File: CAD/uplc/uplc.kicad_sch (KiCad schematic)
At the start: 32 parts, among them J1 Conn_01x06_Pin, J2 SM12B-GHS-TB(LF)(SN), K1 G6K-2F-Y, K2 G6K-2F-Y, U1 DS8242-33S5, U3 ESP32-C3-WROOM-02, U5 TBD62003AFWG, Y1 32.568khz

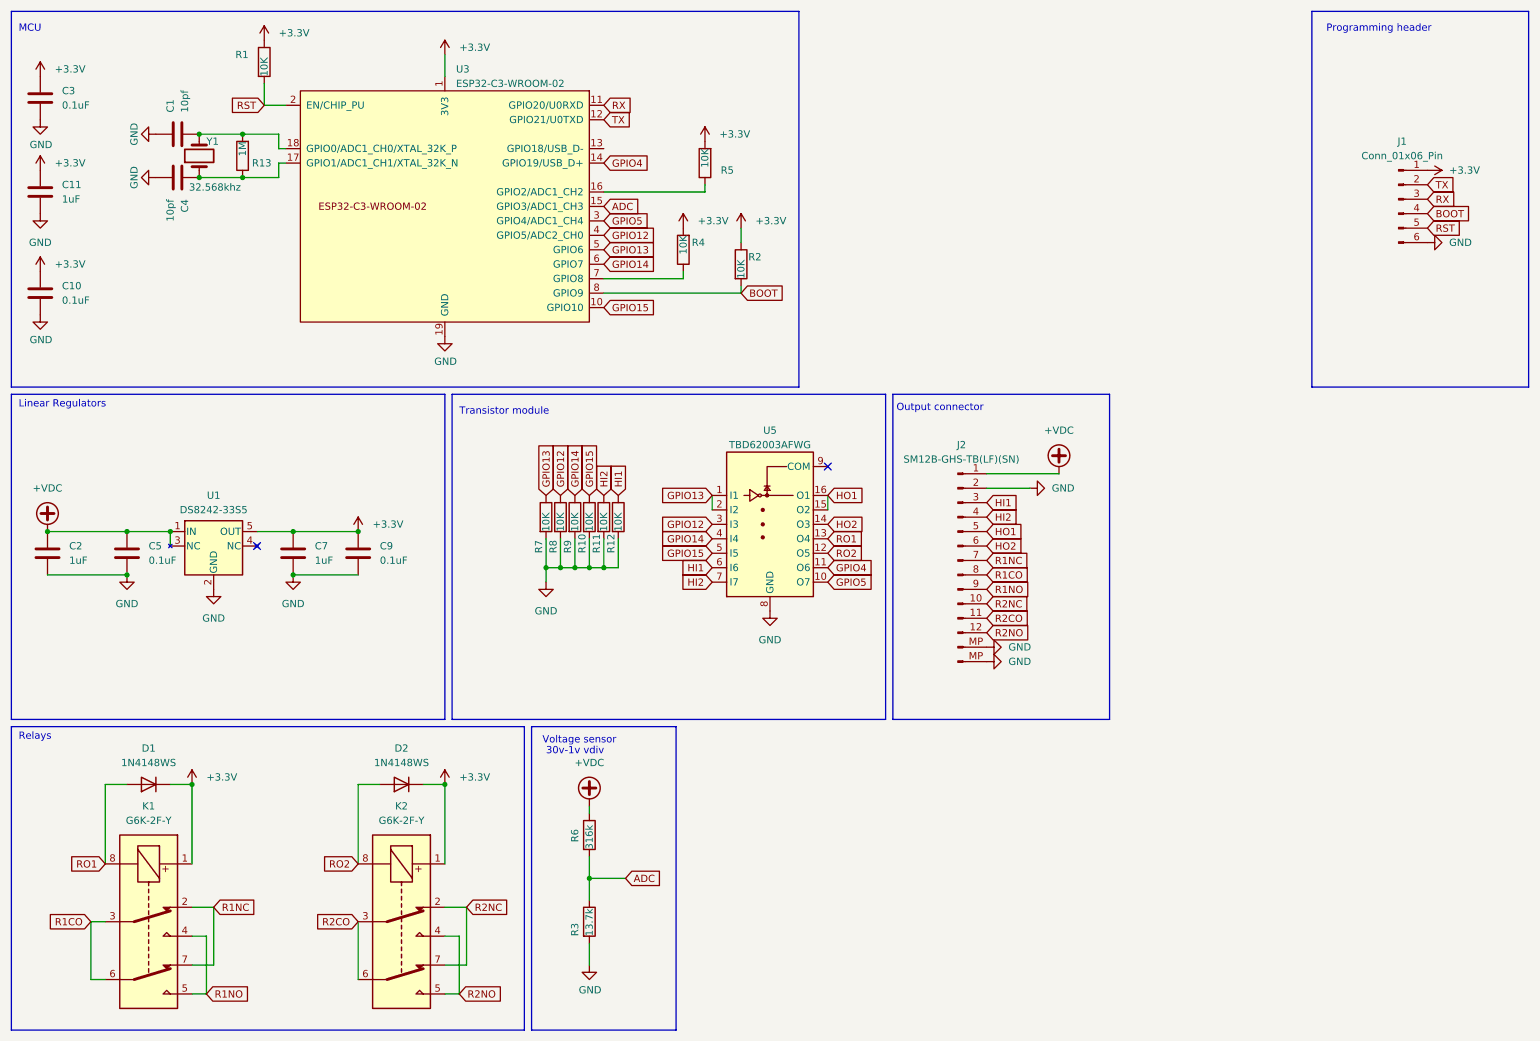
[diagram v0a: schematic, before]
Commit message: Pin Rearangement
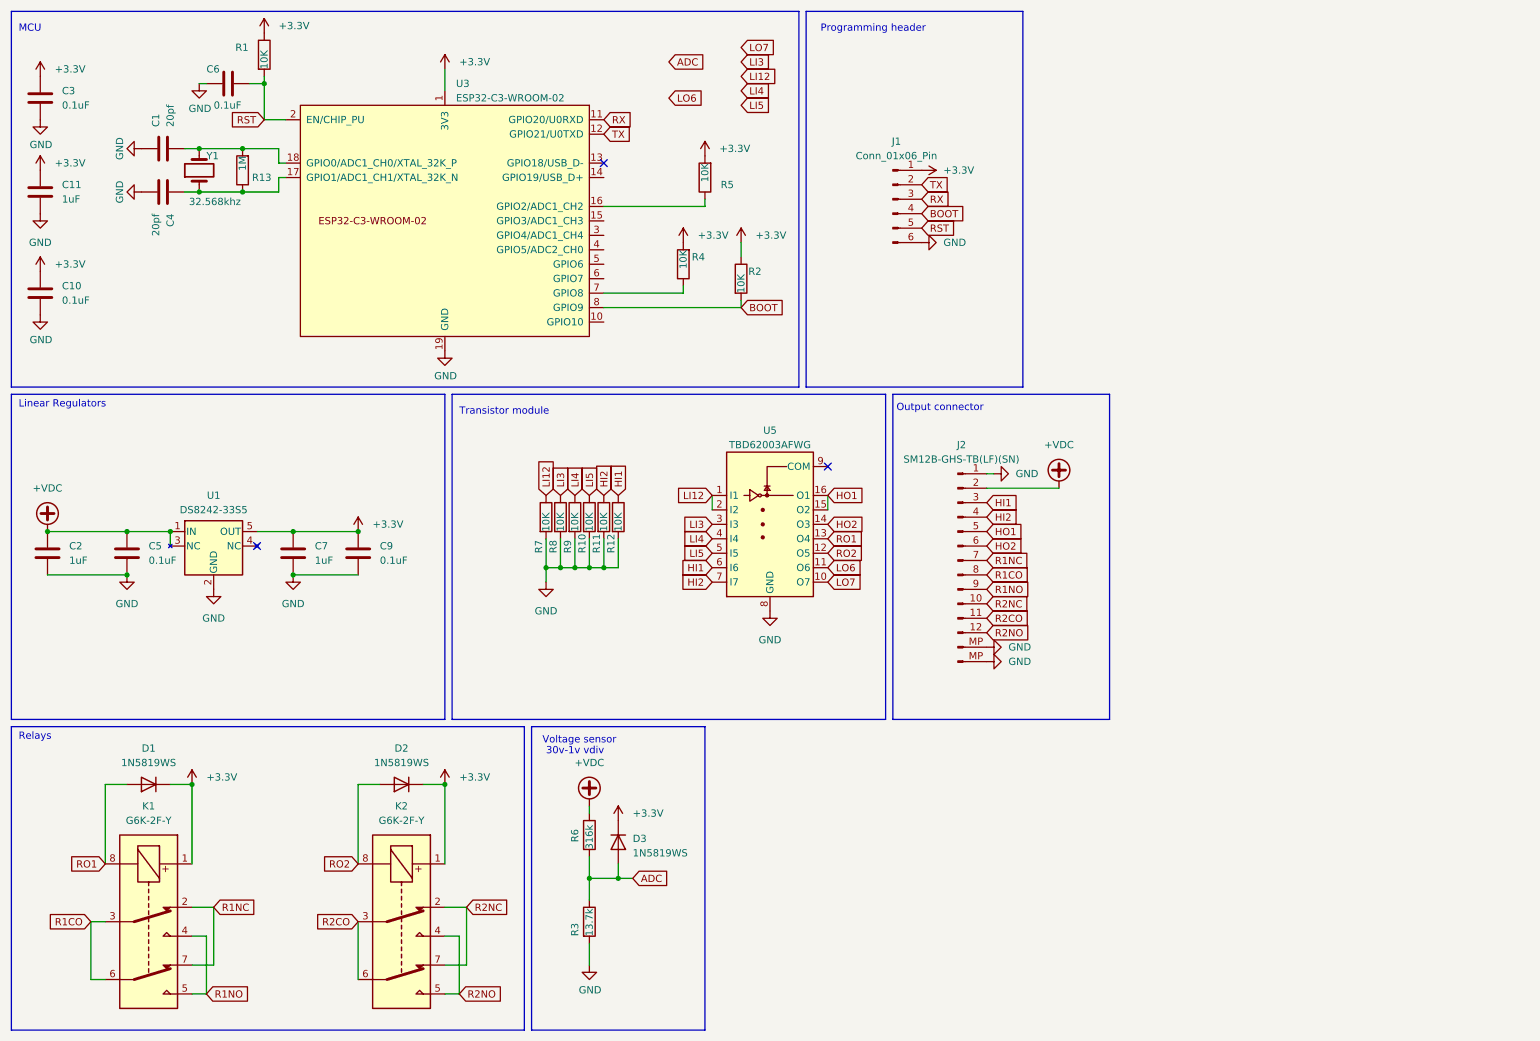
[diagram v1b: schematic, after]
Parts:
- added C6: 0.1uF, Capacitor_SMD:C_0402_1005Metric, symbol esprelay:C
- added D3: 1N5819WS, Diode_SMD:D_SOD-323, symbol esprelay:1N4148WS
- C1, C4: value 10pf -> 20pf; LCSC Part # (none) -> C1554
- D1, D2: value 1N4148WS -> 1N5819WS; LCSC Part # C2128 -> C191023
- R13: LCSC Part # (none) -> C26083
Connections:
- net +3.3V: now also D3.1 (K)
- net +VDC: now also J2.2 (Pin_2); no longer J2.1 (Pin_1)
- net ADC: now also D3.2 (A); no longer U3.15 (GPIO3/ADC1_CH3)
- net GND: now also J2.1 (Pin_1), C6.2; no longer J2.2 (Pin_2)
- net RST: now also C6.1
- net GPIO12 renamed LI3
- net LI3: no longer U3.4 (GPIO5/ADC2_CH0)
- net GPIO13 renamed LI12
- net LI12: no longer U3.5 (GPIO6)
- net GPIO14 renamed LI4
- net LI4: no longer U3.6 (GPIO7)
- net GPIO15 renamed LI5
- net LI5: no longer U3.10 (GPIO10)
- net GPIO4: no longer names the net of U3.14 (GPIO19/USB_D+)
- net GPIO4: no longer U5.11 (O6)
- net GPIO5: no longer names the net of U3.3 (GPIO4/ADC1_CH4)
- net GPIO5: no longer U5.10 (O7)
- new net LO6: U5.11 (O6)
- new net LO7: U5.10 (O7)
- no-connect marks 2 -> 3
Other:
- moved on the sheet: C1, C4, J1, R1, R13, R2, R4, R5, U3, Y1

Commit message: wip
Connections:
- net +VDC: now also J2.12 (Pin_12); no longer J2.2 (Pin_2)
- net ADC: now also U3.3 (GPIO4/ADC1_CH4)
- net BOOT: now also J1.3 (Pin_3); no longer J1.4 (Pin_4)
- net GND: now also J1.2 (Pin_2), J2.11 (Pin_11); no longer J1.6 (Pin_6), J2.1 (Pin_1)
- net HI1: now also J2.8 (Pin_8); no longer J2.3 (Pin_3)
- net HI2: now also J2.7 (Pin_7); no longer J2.4 (Pin_4)
- net HO1: now also J2.10 (Pin_10); no longer J2.5 (Pin_5)
- net HO2: now also J2.9 (Pin_9); no longer J2.6 (Pin_6)
- net LI12: now also U3.6 (GPIO7)
- net LI3: now also U3.15 (GPIO3/ADC1_CH3)
- net LI4: now also U3.4 (GPIO5/ADC2_CH0)
- net LI5: now also U3.5 (GPIO6)
- net LO6: now also U3.13 (GPIO18/USB_D-)
- net LO7: now also U3.14 (GPIO19/USB_D+)
- net R1CO: now also J2.5 (Pin_5); no longer J2.8 (Pin_8)
- net R1NC: now also J2.6 (Pin_6); no longer J2.7 (Pin_7)
- net R1NO: now also J2.4 (Pin_4); no longer J2.9 (Pin_9)
- net R2CO: now also J2.2 (Pin_2); no longer J2.11 (Pin_11)
- net R2NC: now also J2.3 (Pin_3); no longer J2.10 (Pin_10)
- net R2NO: now also J2.1 (Pin_1); no longer J2.12 (Pin_12)
- net RO1: now also U5.12 (O5); no longer U5.13 (O4)
- net RO2: now also U5.13 (O4); no longer U5.12 (O5)
- net RST: now also J1.4 (Pin_4); no longer J1.5 (Pin_5)
- net RX: now also J1.6 (Pin_6); no longer J1.3 (Pin_3)
- net TX: now also J1.5 (Pin_5); no longer J1.2 (Pin_2)
- no-connect marks 3 -> 2

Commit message: Rev 1.0
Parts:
- C1, C10, C11, C2, C3, C4, C5, C6, C7, C9: symbol esprelay:C -> Library:C
- D1, D2, D3: symbol esprelay:1N4148WS -> Library:1N4148WS
- J1: symbol esprelay:Conn_01x06_Pin -> Library:Conn_01x06_Pin
- J2: symbol esprelay:Conn_01x14_Pin -> Library:Conn_01x14_Pin
- K1, K2: symbol esprelay:G6K-2 -> Library:G6K-2
- R1, R10, R11, R12, R2, R3, R4, R5, R6, R7, R8, R9: symbol esprelay:R -> Library:R
- R13: symbol esprelay:R -> Library:R; now not fitted
- U1: symbol esprelay:DS8242 -> Library:DS8242
- U3: footprint Espressif:ESP32-C3-WROOM-02 -> PCM_Espressif:ESP32-C3-WROOM-02; symbol Espressif:ESP32-C3-WROOM-02 -> Library:ESP32-C3-WROOM-02
- U5: symbol esprelay:ULN2003A -> Library:ULN2003A
- Y1: symbol Device:Crystal -> Library:Crystal
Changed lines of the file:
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@@
     )
   )
-  (symbol (lib_id "esprelay:1N4148WS") (at 40.64 152.4 180) (unit 1)
+  (symbol (lib_id "Library:1N4148WS") (at 40.64 152.4 180) (unit 1)
     (in_bom yes) (on_board yes) (dnp no) (fields_autoplaced)
     (property "Reference" "D1" (at 40.64 146.05 0)
@@
     )
   )
-  (symbol (lib_id "esprelay:R") (at 138.43 45.72 180) (unit 1)
+  (symbol (lib_id "Library:R") (at 138.43 45.72 180) (unit 1)
     (in_bom yes) (on_board yes) (dnp no)
     (property "Reference" "R5" (at 143.51 46.99 0)
@@
     )
   )
-  (symbol (lib_id "Espressif:ESP32-C3-WROOM-02") (at 92.71 53.34 0) (unit 1)
+  (symbol (lib_id "Library:ESP32-C3-WROOM-02") (at 92.71 53.34 0) (unit 1)
     (in_bom yes) (on_board yes) (dnp no) (fields_autoplaced)
     (property "Reference" "U3" (at 94.6659 29.21 0)
@@
       (effects (font (size 1.27 1.27)) (justify left))
     )
-    (property "Footprint" "Espressif:ESP32-C3-WROOM-02" (at 92.71 83.82 0)
+    (property "Footprint" "PCM_Espressif:ESP32-C3-WROOM-02" (at 92.71 83.82 0)
       (effects (font (size 1.27 1.27)) hide)
     )
@@
     )
   )
-  (symbol (lib_id "esprelay:R") (at 115.57 105.41 0) (unit 1)
+  (symbol (lib_id "Library:R") (at 115.57 105.41 0) (unit 1)
     (in_bom yes) (on_board yes) (dnp no)
     (property "Reference" "R9" (at 114.3 111.76 90)
@@
     )
   )
-  (symbol (lib_id "esprelay:G6K-2") (at 85.09 176.53 270) (unit 1)
+  (symbol (lib_id "Library:G6K-2") (at 85.09 176.53 270) (unit 1)
     (in_bom yes) (on_board yes) (dnp no) (fields_autoplaced)
     (property "Reference" "K2" (at 85.09 156.21 90)
@@
     )
   )
-  (symbol (lib_id "esprelay:C") (at 43.18 48.26 270) (unit 1)
+  (symbol (lib_id "Library:C") (at 43.18 48.26 270) (unit 1)
     (in_bom yes) (on_board yes) (dnp no) (fields_autoplaced)
     (property "Reference" "C4" (at 44.45 52.07 0)
@@
     )
   )
-  (symbol (lib_id "esprelay:R") (at 57.15 44.45 180) (unit 1)
-    (in_bom yes) (on_board yes) (dnp no)
+  (symbol (lib_id "Library:R") (at 57.15 44.45 180) (unit 1)
+    (in_bom yes) (on_board yes) (dnp yes)
     (property "Reference" "R13" (at 62.23 45.72 0)
       (effects (font (size 1.27 1.27)) (justify left))
@@
     )
   )
-  (symbol (lib_id "esprelay:C") (at 54.61 29.21 270) (unit 1)
+  (symbol (lib_id "Library:C") (at 54.61 29.21 270) (unit 1)
     (in_bom yes) (on_board yes) (dnp no)
     (property "Reference" "C6" (at 50.8 26.67 90)
@@
     )
   )
-  (symbol (lib_id "esprelay:R") (at 118.11 105.41 0) (unit 1)
+  (symbol (lib_id "Library:R") (at 118.11 105.41 0) (unit 1)
     (in_bom yes) (on_board yes) (dnp no)
     (property "Reference" "R10" (at 116.84 111.76 90)
@@
     )
   )
-  (symbol (lib_id "esprelay:C") (at 22.86 111.76 0) (unit 1)
+  (symbol (lib_id "Library:C") (at 22.86 111.76 0) (unit 1)
     (in_bom yes) (on_board yes) (dnp no) (fields_autoplaced)
     (property "Reference" "C2" (at 26.67 110.4899 0)
@@
     )
   )
-  (symbol (lib_id "esprelay:C") (at 36.83 111.76 180) (unit 1)
+  (symbol (lib_id "Library:C") (at 36.83 111.76 180) (unit 1)
     (in_bom yes) (on_board yes) (dnp no) (fields_autoplaced)
     (property "Reference" "C5" (at 40.64 110.49 0)
@@
     )
   )
-  (symbol (lib_id "esprelay:R") (at 123.19 105.41 0) (unit 1)
+  (symbol (lib_id "Library:R") (at 123.19 105.41 0) (unit 1)
     (in_bom yes) (on_board yes) (dnp no)
     (property "Reference" "R12" (at 121.92 111.76 90)
@@
     )
   )
-  (symbol (lib_id "esprelay:DS8242") (at 52.07 110.49 0) (unit 1)
+  (symbol (lib_id "Library:DS8242") (at 52.07 110.49 0) (unit 1)
     (in_bom yes) (on_board yes) (dnp no) (fields_autoplaced)
     (property "Reference" "U1" (at 52.07 101.6 0)
@@
     )
   )
-  (symbol (lib_id "esprelay:R") (at 120.65 105.41 0) (unit 1)
+  (symbol (lib_id "Library:R") (at 120.65 105.41 0) (unit 1)
     (in_bom yes) (on_board yes) (dnp no)
     (property "Reference" "R11" (at 119.38 111.76 90)
@@
     )
   )
-  (symbol (lib_id "esprelay:C") (at 43.18 40.64 90) (unit 1)
+  (symbol (lib_id "Library:C") (at 43.18 40.64 90) (unit 1)
     (in_bom yes) (on_board yes) (dnp no) (fields_autoplaced)
     (property "Reference" "C1" (at 41.91 36.83 0)
@@
     )
   )
-  (symbol (lib_id "esprelay:R") (at 60.96 24.13 0) (unit 1)
+  (symbol (lib_id "Library:R") (at 60.96 24.13 0) (unit 1)
     (in_bom yes) (on_board yes) (dnp no)
     (property "Reference" "R1" (at 55.88 22.86 0)
@@
     )
   )
-  (symbol (lib_id "esprelay:C") (at 66.04 111.76 0) (unit 1)
+  (symbol (lib_id "Library:C") (at 66.04 111.76 0) (unit 1)
     (in_bom yes) (on_board yes) (dnp no) (fields_autoplaced)
     (property "Reference" "C7" (at 69.85 110.4899 0)
@@
     )
   )
-  (symbol (lib_id "esprelay:C") (at 21.59 31.75 0) (unit 1)
+  (symbol (lib_id "Library:C") (at 21.59 31.75 0) (unit 1)
     (in_bom yes) (on_board yes) (dnp no) (fields_autoplaced)
     (property "Reference" "C3" (at 25.4 30.48 0)
@@
     )
   )
-  (symbol (lib_id "esprelay:R") (at 134.62 60.96 180) (unit 1)
+  (symbol (lib_id "Library:R") (at 134.62 60.96 180) (unit 1)
     (in_bom yes) (on_board yes) (dnp no)
     (property "Reference" "R4" (at 138.43 59.69 0)
@@
     )
   )
-  (symbol (lib_id "esprelay:R") (at 118.11 161.29 0) (unit 1)
+  (symbol (lib_id "Library:R") (at 118.11 161.29 0) (unit 1)
     (in_bom yes) (on_board yes) (dnp no)
     (property "Reference" "R6" (at 115.57 162.56 90)
@@
     )
   )
-  (symbol (lib_id "esprelay:C") (at 21.59 48.26 0) (unit 1)
+  (symbol (lib_id "Library:C") (at 21.59 48.26 0) (unit 1)
     (in_bom yes) (on_board yes) (dnp no) (fields_autoplaced)
     (property "Reference" "C11" (at 25.4 46.9899 0)
@@
     )
   )
-  (symbol (lib_id "esprelay:C") (at 77.47 111.76 0) (unit 1)
+  (symbol (lib_id "Library:C") (at 77.47 111.76 0) (unit 1)
     (in_bom yes) (on_board yes) (dnp no) (fields_autoplaced)
     (property "Reference" "C9" (at 81.28 110.49 0)
@@
     )
   )
-  (symbol (lib_id "esprelay:Conn_01x14_Pin") (at 182.88 113.03 0) (unit 1)
+  (symbol (lib_id "Library:Conn_01x14_Pin") (at 182.88 113.03 0) (unit 1)
     (in_bom yes) (on_board yes) (dnp no) (fields_autoplaced)
     (property "Reference" "J2" (at 183.515 92.71 0)
@@
     )
   )
-  (symbol (lib_id "esprelay:1N4148WS") (at 123.19 162.56 270) (unit 1)
+  (symbol (lib_id "Library:1N4148WS") (at 123.19 162.56 270) (unit 1)
     (in_bom yes) (on_board yes) (dnp no) (fields_autoplaced)
     (property "Reference" "D3" (at 125.73 161.925 90)
@@
     )
   )
-  (symbol (lib_id "esprelay:C") (at 21.59 66.04 0) (unit 1)
+  (symbol (lib_id "Library:C") (at 21.59 66.04 0) (unit 1)
     (in_bom yes) (on_board yes) (dnp no) (fields_autoplaced)
     (property "Reference" "C10" (at 25.4 64.77 0)
@@
     )
   )
-  (symbol (lib_id "esprelay:Conn_01x06_Pin") (at 171.45 49.53 0) (unit 1)
+  (symbol (lib_id "Library:Conn_01x06_Pin") (at 171.45 49.53 0) (unit 1)
     (in_bom yes) (on_board yes) (dnp no) (fields_autoplaced)
     (property "Reference" "J1" (at 172.085 39.37 0)
@@
     )
   )
-  (symbol (lib_id "esprelay:R") (at 113.03 105.41 0) (unit 1)
+  (symbol (lib_id "Library:R") (at 113.03 105.41 0) (unit 1)
     (in_bom yes) (on_board yes) (dnp no)
     (property "Reference" "R8" (at 111.76 111.76 90)
@@
     )
   )
-  (symbol (lib_id "esprelay:R") (at 110.49 105.41 0) (unit 1)
+  (symbol (lib_id "Library:R") (at 110.49 105.41 0) (unit 1)
     (in_bom yes) (on_board yes) (dnp no)
     (property "Reference" "R7" (at 109.22 111.76 90)
@@
     )
   )
-  (symbol (lib_id "esprelay:R") (at 118.11 176.53 0) (unit 1)
+  (symbol (lib_id "Library:R") (at 118.11 176.53 0) (unit 1)
     (in_bom yes) (on_board yes) (dnp no)
     (property "Reference" "R3" (at 115.57 179.07 90)
@@
     )
   )
-  (symbol (lib_id "Device:Crystal") (at 49.53 44.45 90) (unit 1)
+  (symbol (lib_id "Library:Crystal") (at 49.53 44.45 90) (unit 1)
     (in_bom yes) (on_board yes) (dnp no)
     (property "Reference" "Y1" (at 50.8 41.91 90)
@@
       (effects (font (size 1.27 1.27)) hide)
     )
-    (property "Datasheet" "https://datasheet.lcsc.com/lcsc/1810171817_Seiko-Epson-Q13FC13500004_C32346.pdf" (at 49.53 44.45 0)
+    (property "Datasheet" "~" (at 49.53 44.45 0)
       (effects (font (size 1.27 1.27)) hide)
     )
@@
     )
   )
-  (symbol (lib_id "esprelay:ULN2003A") (at 149.86 106.68 0) (unit 1)
+  (symbol (lib_id "Library:ULN2003A") (at 149.86 106.68 0) (unit 1)
     (in_bom yes) (on_board yes) (dnp no) (fields_autoplaced)
     (property "Reference" "U5" (at 149.86 90.17 0)
@@
     )
   )
-  (symbol (lib_id "esprelay:R") (at 144.78 63.5 0) (unit 1)
+  (symbol (lib_id "Library:R") (at 144.78 63.5 0) (unit 1)
     (in_bom yes) (on_board yes) (dnp no)
     (property "Reference" "R2" (at 146.05 62.23 0)
@@
     )
   )
-  (symbol (lib_id "esprelay:1N4148WS") (at 85.09 152.4 180) (unit 1)
+  (symbol (lib_id "Library:1N4148WS") (at 85.09 152.4 180) (unit 1)
     (in_bom yes) (on_board yes) (dnp no) (fields_autoplaced)
     (property "Reference" "D2" (at 85.09 146.05 0)
@@
     )
   )
-  (symbol (lib_id "esprelay:G6K-2") (at 40.64 176.53 270) (unit 1)
+  (symbol (lib_id "Library:G6K-2") (at 40.64 176.53 270) (unit 1)
     (in_bom yes) (on_board yes) (dnp no) (fields_autoplaced)
     (property "Reference" "K1" (at 40.64 156.21 90)
